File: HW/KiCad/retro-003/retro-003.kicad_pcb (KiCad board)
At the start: 4 copper layers, 100 x 100 mm, 297 parts, among them J1 ATF_JTAG, J100 x, J101 x, J102 x, J103 x, J104 x, J105 x, J106 x, J12 Reset, J2 Conn_02x04_Top_Bottom, J21 x, J22 x, J3 Serial, J37 x, J38 x, J39 x, J4 SysBus, J40 x, J41 x, J42 x, J43 x, J44 x, J45 x, J46 x, J47 x, J48 x, J49 x, J5 x, J50 x, J51 x, J52 x, J53 x, J54 x, J55 x, J56 x, J57 x, J58 x, J59 x, J6 SysBus, J60 x, J61 x, J62 x, J63 x, J64 x, J65 x, J66 x, J67 x, J68 x, J69 x, J7 Conn_01x16_Pin, J70 x, J71 x, J72 x, J73 x, J74 x, J75 x, J76 x, J77 x, J78 x, J79 x, J8 x, J80 x, J81 x, J82 x, J83 x, J84 x, J85 x, J86 x, J87 x, J88 x, J89 x, J90 x, J91 x, J92 x, J93 x, J94 x, J95 x, J96 x, J97 x, J98 x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

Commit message: PCB send to JLCpcb (with prev git number)
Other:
- board text added: "PCB v.1.0"
- board text added: "git: 91f4cbe"
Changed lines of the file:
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@@
 			(plot_on_all_layers_selection 0x00000000_00000000_00000000_00000000)
 			(disableapertmacros no)
-			(usegerberextensions no)
-			(usegerberattributes no)
+			(usegerberextensions yes)
+			(usegerberattributes yes)
 			(usegerberadvancedattributes yes)
-			(creategerberjobfile yes)
+			(creategerberjobfile no)
 			(dashed_line_dash_ratio 12.000000)
 			(dashed_line_gap_ratio 3.000000)
@@
 		)
 	)
+	(gr_text "git: 91f4cbe"
+		(at 173.6471 78.20152 90)
+		(layer "B.SilkS")
+		(effects
+			(font
+				(size 2 2)
+				(thickness 0.4)
+				(bold yes)
+			)
+			(justify left bottom mirror)
+		)
+	)
 	(gr_text "Data"
 		(at 156.718 39.7256 90)
@@
 		(layer "B.SilkS")
 		(effects
+			(font
+				(size 2 2)
+				(thickness 0.4)
+				(bold yes)
+			)
+			(justify left bottom mirror)
+		)
+	)
+	(gr_text "PCB v.1.0"
+		(at 167.62476 97.78365 90)
+		(layer "B.SilkS")
+		(effects

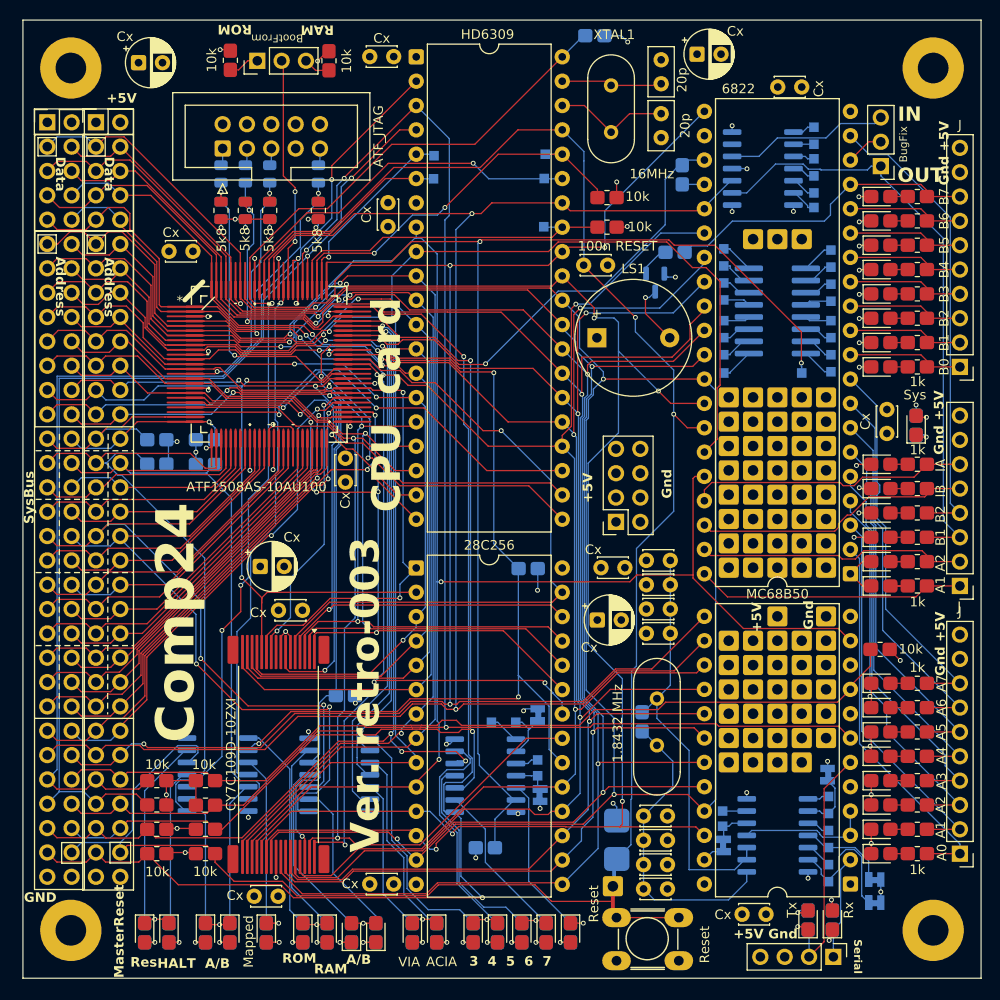
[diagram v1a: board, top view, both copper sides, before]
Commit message: fixed polarity of IRQ, FIRQ, ... pins
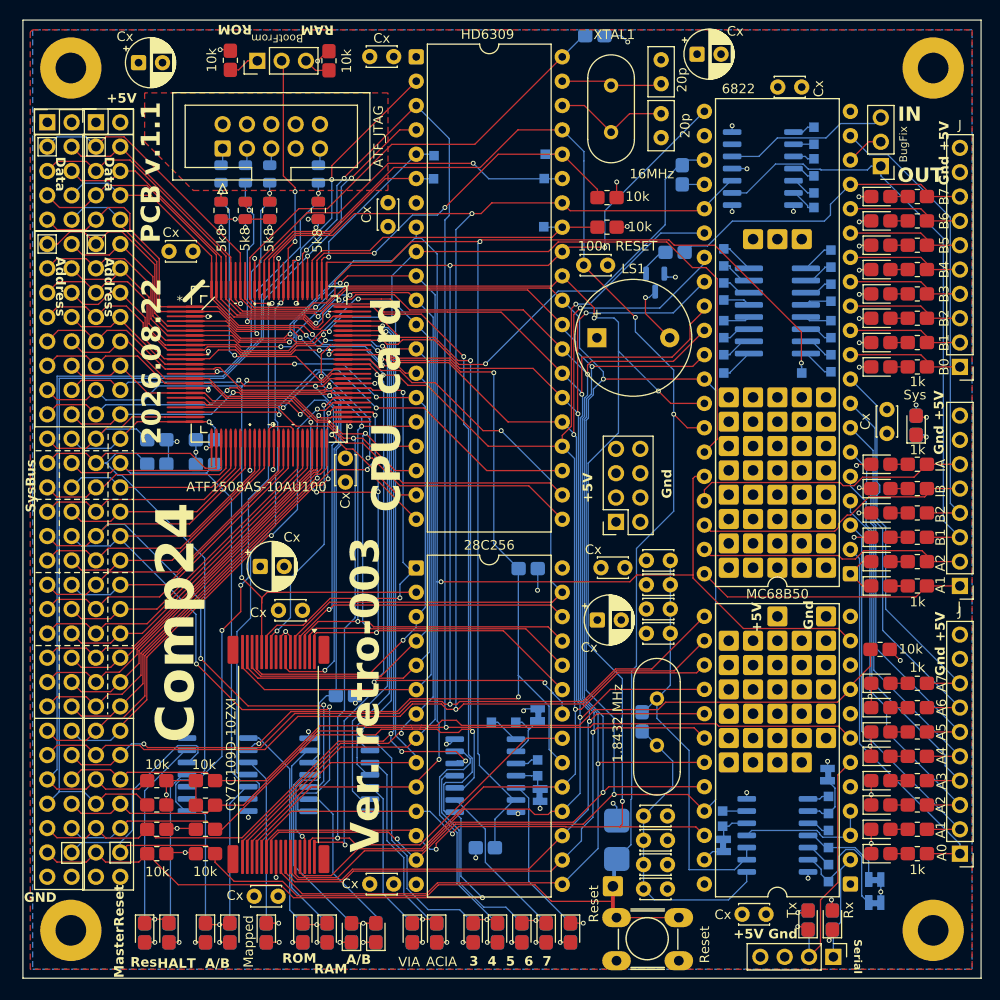
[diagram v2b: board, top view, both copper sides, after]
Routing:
- added copper zone on B.Cu, net (none)
- added copper zone on F.Cu, net (none)
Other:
- board text added: "2026.08.22"
- board text added: "PCB v.1.1"
- board text added: "git: eb87ef2+"
- board text removed: "2026.08.20"
- board text removed: "PCB v.1.0"
- board text removed: "git: 91f4cbe"
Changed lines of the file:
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@@
 		)
 		(property "Value" "SysBus"
-			(at -6.98 39.0602 90)
+			(at -6.7768 38.4506 90)
 			(unlocked yes)
 			(layer "B.SilkS")
@@
 		)
 		(property "Value" "SysBus"
-			(at -1.8996 39.1464 90)
+			(at -1.7218 37.9526 90)
 			(unlocked yes)
 			(layer "F.SilkS")
@@
 		)
 	)
+	(gr_text "2026.08.22"
+		(at 167.005 69.6976 90)
+		(layer "F.SilkS")
+		(effects
+			(font
+				(size 2 2)
+				(thickness 0.4)
+				(bold yes)
+			)
+			(justify left bottom)
+		)
+	)
 	(gr_text "RAM"
 		(at 182.7784 125.0188 0)
@@
 		)
 	)
+	(gr_text "PCB v.1.1"
+		(at 166.9288 48.6664 90)
+		(layer "F.SilkS")
+		(effects
+			(font
+				(size 2 2)
+				(thickness 0.4)
+				(bold yes)
+			)
+			(justify left bottom)
+		)
+	)
 	(gr_text "115.200 Baud"
 		(at 247.85574 94.07652 90)
@@
 		)
 	)
-	(gr_text "git: 91f4cbe"
-		(at 173.6471 78.20152 90)
+	(gr_text "git: eb87ef2+"
+		(at 173.4693 76.88072 90)
 		(layer "B.SilkS")
 		(effects
@@
 		)
 	)
-	(gr_text "2026.08.20"
+	(gr_text "2026.08.22"
 		(at 168.55186 78.98257 90)
 		(layer "B.SilkS")
@@
 		)
 	)
-	(gr_text "PCB v.1.0"
+	(gr_text "PCB v.1.1"
 		(at 167.62476 97.78365 90)
 		(layer "B.SilkS")
@@
 	)
 	(segment
-		(start 236.0185 121.5881)
-		(end 236.0185 105.6115)
+		(start 237.44682 104.18318)
+		(end 238.76 102.87)
+		(width 0.1016)
+		(layer "F.Cu")
+		(net 148)
+	)
+	(segment
+		(start 235.63834 117.22989)
+		(end 237.44682 115.42141)
 		(width 0.1016)
 		(layer "F.Cu")
@@
 	)
 	(segment
-		(start 236.0185 105.6115)
-		(end 238.76 102.87)
+		(start 237.44682 115.42141)
+		(end 237.44682 104.18318)
 		(width 0.1016)
 		(layer "F.Cu")
@@
 	(segment
 		(start 234.442 123.1646)
-		(end 236.0185 121.5881)
+		(end 235.63834 121.96826)
+		(width 0.1016)
+		(layer "F.Cu")
+		(net 148)
+	)
+	(segment
+		(start 235.63834 121.96826)
+		(end 235.63834 117.22989)
 		(width 0.1016)
 		(layer "F.Cu")
@@
 	)
 	(segment
+		(start 165.9636 52.1716)
+		(end 162.56 48.768)
+		(width 0.1016)
+		(layer "F.Cu")
+		(net 195)
+	)
+	(segment
 		(start 222.2778 51.2316)
 		(end 219.6041 48.5579)
@@
 	)
 	(segment
-		(start 165.9636 52.1716)
-		(end 162.56 48.768)
+		(start 223.52 70.485)
+		(end 224.85604 69.14896)
 		(width 0.1016)
 		(layer "F.Cu")
@@
 	)
 	(segment
-		(start 223.52 70.485)
-		(end 224.8566 69.1484)
+		(start 208.2482 48.5579)
+		(end 207.2507 49.5554)
 		(width 0.1016)
 		(layer "F.Cu")
@@
 	)
 	(segment
-		(start 225.0904 63.5666)
-		(end 225.1589 63.4981)
+		(start 207.2507 49.5554)
+		(end 193.4464 49.5554)
 		(width 0.1016)
 		(layer "F.Cu")
@@
 	)
 	(segment
-		(start 224.8566 63.795978)
-		(end 225.085978 63.5666)
-		(width 0.1016)
-		(layer "F.Cu")
-		(net 195)
-	)
-	(segment
 		(start 180.467 58.5978)
 		(end 180.840355 58.971155)
@@
 	)
 	(segment
-		(start 174.03076 57.8148)
-		(end 175.022199 58.806239)
+		(start 223.6961 51.2316)
+		(end 222.2778 51.2316)
 		(width 0.1016)
 		(layer "F.Cu")
@@
 	)
 	(segment
-		(start 225.1589 52.6944)
-		(end 223.6961 51.2316)
+		(start 174.03076 57.8148)
+		(end 175.022199 58.806239)
 		(width 0.1016)
 		(layer "F.Cu")
@@
 	)
 	(segment
-		(start 225.085978 63.5666)
-		(end 225.0904 63.5666)
-		(width 0.1016)
-		(layer "F.Cu")
-		(net 195)
-	)
-	(segment
-		(start 208.2482 48.5579)
-		(end 207.2507 49.5554)
+		(start 219.6041 48.5579)
+		(end 208.2482 48.5579)
 		(width 0.1016)
 		(layer "F.Cu")
@@
 	)
 	(segment
-		(start 224.8566 69.1484)
-		(end 224.8566 63.795978)
-		(width 0.1016)
-		(layer "F.Cu")
-		(net 195)
-	)
-	(segment
 		(start 169.3886 57.8148)
 		(end 174.03076 57.8148)
@@
 	)
 	(segment
-		(start 225.1589 63.4981)
-		(end 225.1589 52.6944)
-		(width 0.1016)
-		(layer "F.Cu")
-		(net 195)
-	)
-	(segment
-		(start 219.6041 48.5579)
-		(end 208.2482 48.5579)
+		(start 224.85604 52.39154)
+		(end 223.6961 51.2316)
 		(width 0.1016)
 		(layer "F.Cu")
@@
 	)
 	(segment
-		(start 223.6961 51.2316)
-		(end 222.2778 51.2316)
+		(start 224.85604 69.14896)
+		(end 224.85604 52.39154)
 		(width 0.1016)
 		(layer "F.Cu")
@@
 	)
 	(segment
-		(start 207.2507 49.5554)
-		(end 193.4464 49.5554)
-		(width 0.1016)
-		(layer "F.Cu")
-		(net 195)
-	)
-	(segment
 		(start 158.623 49.911)
 		(end 161.417 49.911)
@@
 	)
 	(zone
+		(net 0)
+		(net_name "")
+		(layer "F.Cu")
+		(hatch edge 0.5)
+		(priority 7)
+		(connect_pads
+			(clearance 0.5)
+		)
+		(min_thickness 0.25)
+		(filled_areas_thickness no)
+		(fill yes
+			(thermal_gap 0.5)
+			(thermal_bridge_width 0.5)
+			(island_removal_mode 1)
+			(island_area_min 10)
+		)
+		(polygon
+			(pts
+				(xy 153.3906 26.416) (xy 251.46 26.416) (xy 251.46 124.46) (xy 153.162 124.46) (xy 153.162 26.6446)
+			)
+		)
+	)
+	(zone
+		(net 0)
+		(net_name "")
+		(layer "F.Cu")
+		(hatch edge 0.5)
+		(priority 6)
+		(connect_pads
+			(clearance 0.5)
+		)
+		(min_thickness 0.25)
+		(filled_areas_thickness no)
+		(fill yes
+			(thermal_gap 0.5)
+			(thermal_bridge_width 0.5)
+			(island_removal_mode 1)
+			(island_area_min 10)
+		)
+		(polygon
+			(pts
+				(xy 170.18 43.18) (xy 190.5 43.18) (xy 190.5 33.02) (xy 190.4746 32.9946) (xy 165.1 32.9946) (xy 165.1 38.1)
+			)
+		)
+	)
+	(zone
+		(net 0)
+		(net_name "")
+		(layer "B.Cu")
+		(hatch edge 0.5)
+		(priority 2)
+		(connect_pads
+			(clearance 0.5)
+		)
+		(min_thickness 0.25)
+		(filled_areas_thickness no)
+		(fill yes
+			(thermal_gap 0.5)
+			(thermal_bridge_width 0.5)
+			(island_removal_mode 1)
+			(island_area_min 10)
+		)
+		(polygon
+			(pts
+				(xy 251.46 26.416) (xy 153.416 26.416) (xy 153.416 124.46) (xy 251.46 124.46)
+			)
+		)
+	)
+	(zone

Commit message: fixed PCB send to JLCpcb (with prev git number) - flood copper on outside
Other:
- board text added: "git: acebbbb+"
- board text removed: "git: eb87ef2+"
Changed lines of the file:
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@@
 		)
 	)
-	(gr_text "git: eb87ef2+"
+	(gr_text "git: acebbbb+"
 		(at 173.4693 76.88072 90)
 		(layer "B.SilkS")
